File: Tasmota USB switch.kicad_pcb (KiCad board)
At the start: 2 copper layers, 54.6 x 25.4 mm, 6 parts, among them J1 USB_A, J2 USB_A, J3 Conn_01x06_Female, Q1 2N7000, SW1 SW_Push, U1 ESP-01v090

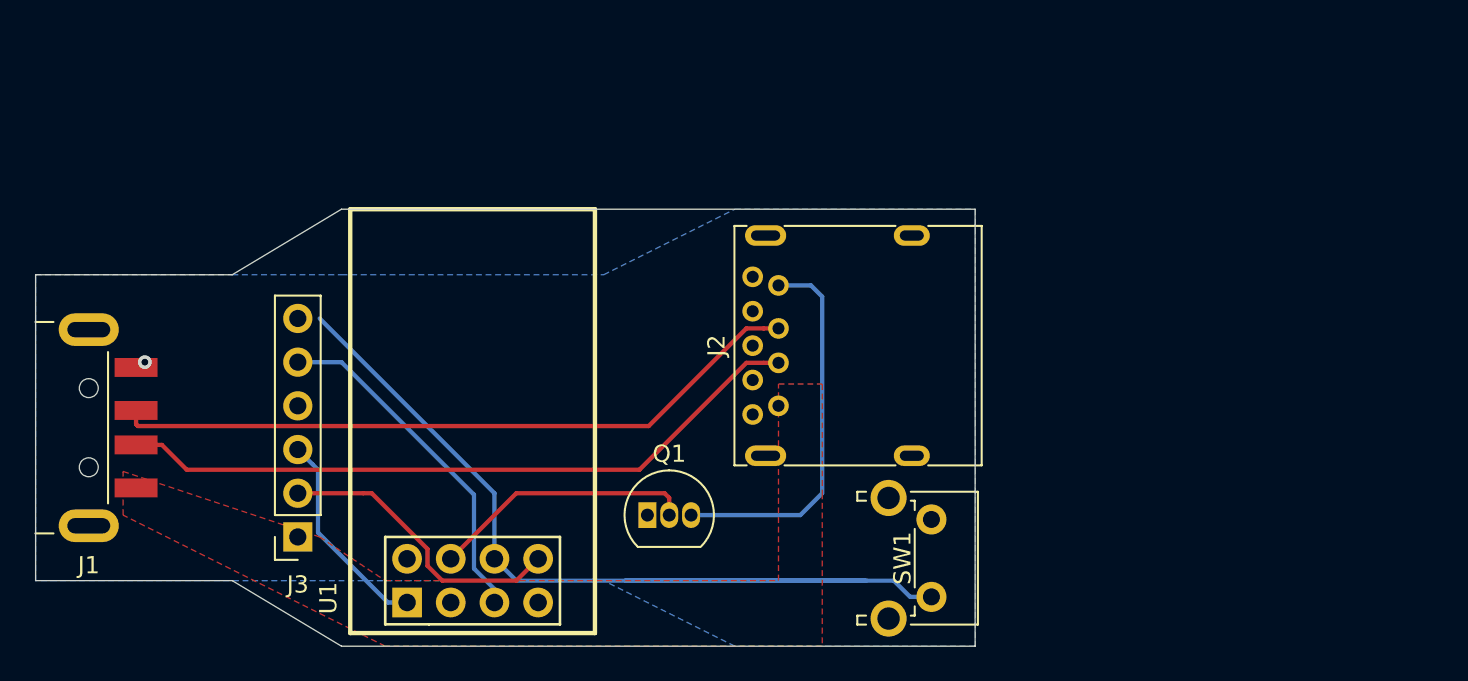
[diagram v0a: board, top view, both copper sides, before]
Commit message: V0.0.2
Now with the missing Voltage regulator!!!
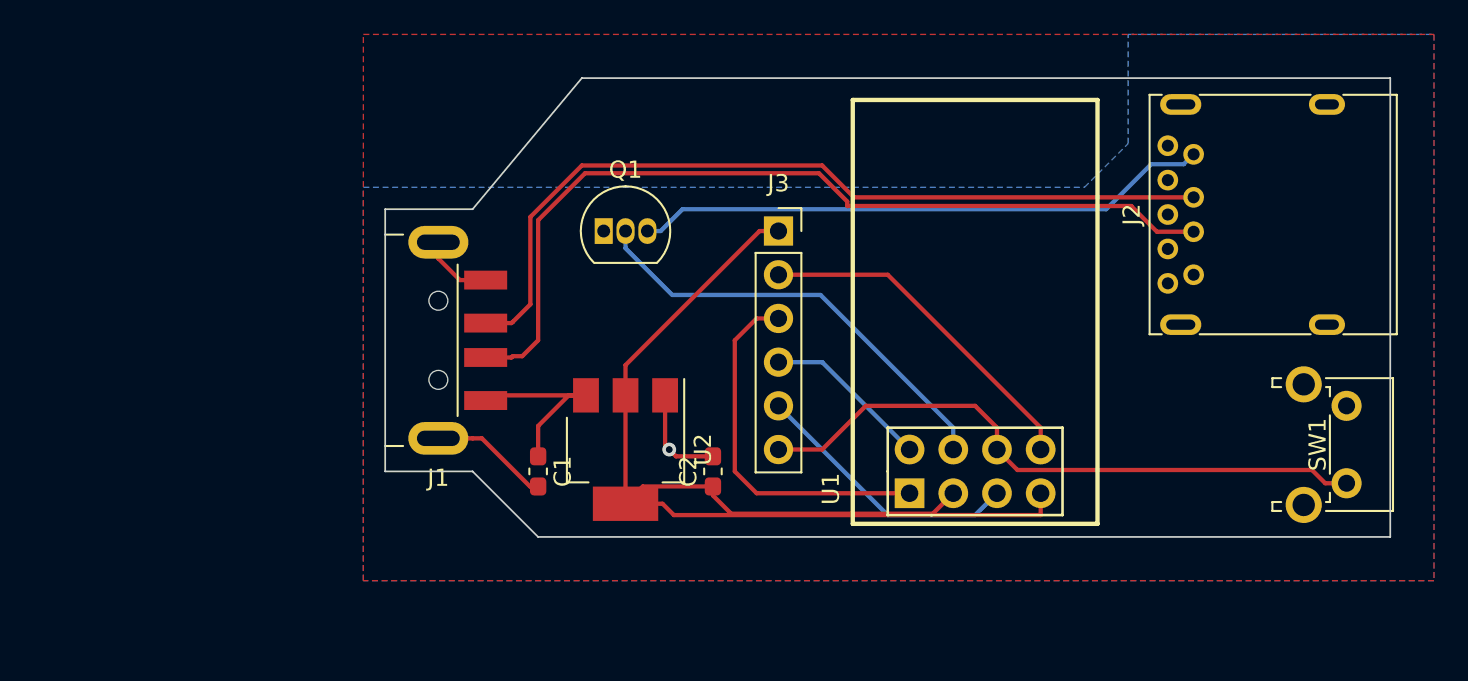
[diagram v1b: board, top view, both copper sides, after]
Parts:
- added C1: C, Capacitor_SMD:C_0603_1608Metric_Pad1.05x0.95mm_HandSolder, F.Cu at (141.0, 102.9)
- added C2: C, Capacitor_SMD:C_0603_1608Metric_Pad1.05x0.95mm_HandSolder, F.Cu at (151.1, 102.9)
- added U2: AMS1117-3.3, Package_TO_SOT_SMD:SOT-223-3_TabPin2, F.Cu at (146.1, 101.6)
- moved J3 33.1 mm to (154.9, 88.9), turned to 0 degrees
- moved U1 29.9 mm to (162.6, 104.1)
- moved J2 25.3 mm to (179.1, 91.4)
- moved SW1 25.0 mm to (188.0, 99.1)
- moved J1 20.9 mm to (128.3, 95.2)
- moved Q1 16.7 mm to (144.8, 88.9)
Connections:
- J1 pad 1: VCC -> VBUS
- J2 pad 1: VCC -> VBUS
- J3 pad 1: VCC -> Net-(C2-Pad1)
- U1 pad 3: VCC -> Net-(C2-Pad1)
- U1 pad 7: VCC -> Net-(C2-Pad1)
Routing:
- net Net-(C2-Pad1): track 0.00 -> 66.8 mm
- net GND: track 0.00 -> 26.9 mm
- net Net-(J3-Pad6): track 58.5 -> 36.7 mm
- net VBUS: track 0.00 -> 11.2 mm
- net Net-(J2-Pad4): track 22.4 -> 33.6 mm
- net Net-(J1-Pad2): track 40.5 -> 51.2 mm
- net Net-(Q1-Pad2): track 15.4 -> 25.6 mm
- net Net-(J3-Pad3): track 12.2 -> 21.4 mm
- net Net-(J1-Pad3): track 40.5 -> 48.7 mm
- net Net-(J3-Pad5): track 20.2 -> 15.9 mm
- net Net-(J3-Pad2): track 17.2 -> 20.2 mm
- added copper zone on F.Cu, net VBUS
- removed copper zone on F.Cu, net VCC
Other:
- board size 54.6 x 25.4 mm -> 58.4 x 26.7 mm
- rule pad_to_mask_clearance: 0.051 -> 0

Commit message: v0.0.3
Now with blinkenlight
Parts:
- added D1: LED, LED_SMD:LED_0805_2012Metric_Pad1.15x1.40mm_HandSolder, F.Cu at (188.0, 96.5)
- added R1: R, Resistor_SMD:R_0805_2012Metric_Pad1.15x1.40mm_HandSolder, F.Cu at (182.9, 96.5)
- moved Q1 33.7 mm to (176.5, 100.3)
- moved C2 14.5 mm to (147.3, 88.9), turned to 180 degrees
- moved U2 7.73 mm to (147.3, 94.0), turned to 0 degrees
- moved C1 7.41 mm to (147.3, 99.1), turned to 180 degrees
- moved J1 1.27 mm to (128.3, 94.0)
- moved SW1 1.27 mm to (188.0, 100.3)
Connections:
- SW1 pad : GND -> (no net)
- SW1 pad 1: GND -> Net-(J3-Pad6)
- SW1 pad 2: Net-(J3-Pad6) -> GND
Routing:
- net GND: track 26.9 -> 46.8 mm, vias 1 -> 2
- net Net-(C2-Pad1): track 66.8 -> 57.2 mm
- net Net-(Q1-Pad2): track 25.6 -> 18.1 mm
- net VBUS: track 11.2 -> 5.45 mm
- net Net-(J3-Pad6): track 36.7 -> 41.3 mm
- net Net-(D1-Pad1): track 0.00 -> 3.03 mm
- net Net-(J2-Pad4): track 33.6 -> 31.3 mm
- net Net-(J1-Pad3): track 48.7 -> 49.7 mm
- net Net-(J1-Pad2): track 51.2 -> 51.9 mm
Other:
- board size 58.4 x 26.7 mm -> 58.4 x 27.9 mm
- net class Power added: clearance 0.2, trace_width 0.508, via_dia 1.524, via_drill 0.762
